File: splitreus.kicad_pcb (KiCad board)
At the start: 2 copper layers, 134.3 x 107.2 mm, 97 parts, among them J1 TRRS, J2 battery, SW0 SW_PUSH, SW1 SW_PUSH, SW10 SW_PUSH, SW11 SW_PUSH, SW12 SW_PUSH, SW13 SW_PUSH, SW14 SW_PUSH, SW15 SW_PUSH, SW16 SW_PUSH, SW17 SW_PUSH, SW18 SW_PUSH, SW19 SW_PUSH, SW2 SW_PUSH, SW20 SW_PUSH, SW21 SW_PUSH, SW22 SW_PUSH, SW23 SW_PUSH, SW24 SW_PUSH, SW25 SW_PUSH, SW26 SW_PUSH, SW27 SW_PUSH, SW28 SW_PUSH, SW29 SW_PUSH, SW3 SW_PUSH, SW30 SW_PUSH, SW4 SW_PUSH, SW5 SW_PUSH, SW6 SW_PUSH, SW7 SW_PUSH, SW8 SW_PUSH, SW9 SW_PUSH, U1 ProMicro

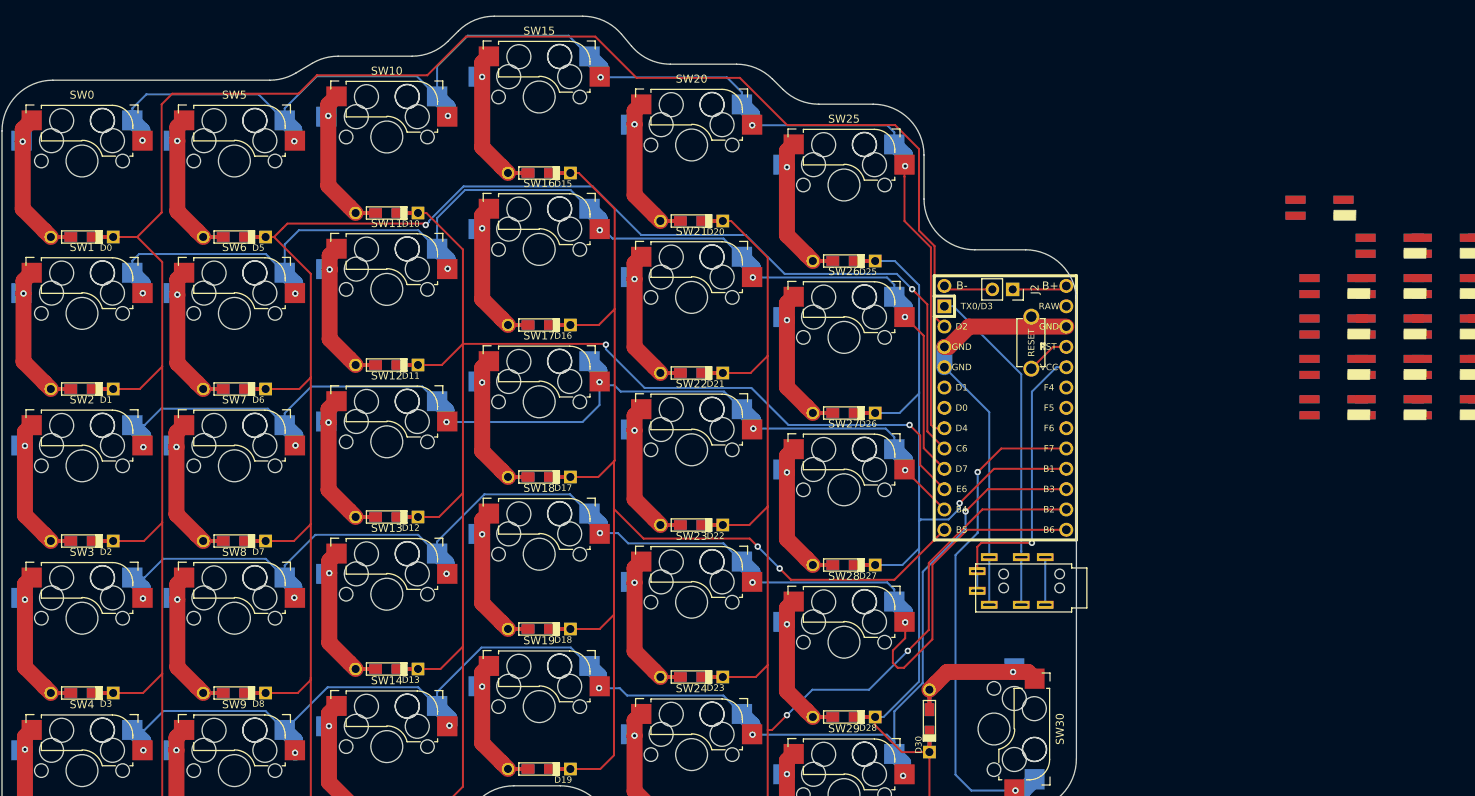
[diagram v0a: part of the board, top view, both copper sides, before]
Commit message: leds and placements
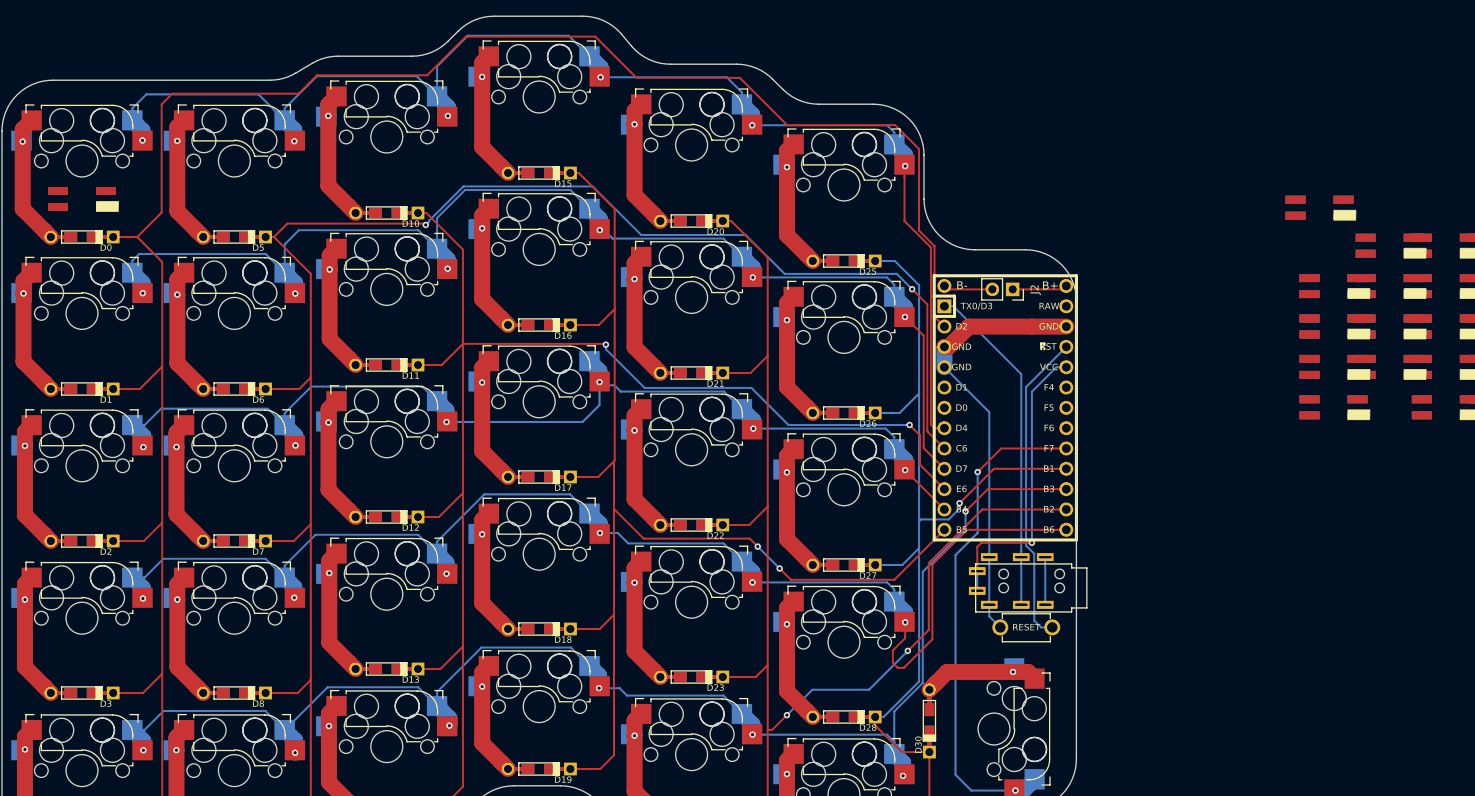
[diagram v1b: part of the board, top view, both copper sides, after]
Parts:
- moved D90 165.5 mm to (0.00, 4.75)
- moved RST1 35.6 mm to (118.0, 58.3), turned to 180 degrees
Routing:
- net RST: track 5.70 -> 39.5 mm
- net GND: track 52.1 -> 54.3 mm

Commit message: leds
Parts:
- moved D94 176.0 mm to (0.00, 81.0)
- moved D99 173.4 mm to (19.1, 81.0)
- moved D92 166.6 mm to (0.00, 42.9)
- moved D93 161.8 mm to (0.00, 61.9)
- moved D91 156.7 mm to (0.00, 23.8)
- moved D98 153.9 mm to (19.1, 42.9)
- moved D95 151.5 mm to (19.1, 4.75)
- moved D97 146.1 mm to (19.1, 42.9)
- moved D96 137.4 mm to (19.1, 23.8)
- moved D912 133.8 mm to (38.1, 39.9)
- moved D910 121.8 mm to (38.1, 1.75)
- moved D916 117.5 mm to (38.1, 20.8)
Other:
- outline, holes or cut-outs redrawn

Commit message: holes and leds
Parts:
- added U1: HOLE, MountingHole:MountingHole_2.2mm_M2_DIN965_Pad, F.Cu at (28.6, 27.1)
- added U2: HOLE, MountingHole:MountingHole_2.2mm_M2_DIN965_Pad, F.Cu at (28.6, 65.2)
- added U3: HOLE, MountingHole:MountingHole_2.2mm_M2_DIN965_Pad, F.Cu at (85.7, 29.1)
- added U4: HOLE, MountingHole:MountingHole_2.2mm_M2_DIN965_Pad, F.Cu at (85.7, 67.2)
- moved D914 161.2 mm to (38.1, 78.0)
- moved D919 148.2 mm to (57.1, 73.0)
- moved D913 146.0 mm to (38.1, 58.9)
- moved D924 140.2 mm to (76.2, 79.0)
- moved D918 133.0 mm to (57.1, 53.9)
- moved D911 125.5 mm to (38.1, 20.8)
- moved D923 123.5 mm to (76.2, 59.9)
- moved D917 121.2 mm to (57.1, 34.9)
- moved D915 117.0 mm to (57.1, -3.25)
- moved D928 114.5 mm to (95.2, 64.9)
- moved D922 110.2 mm to (76.2, 40.9)
- moved D929 103.9 mm to (95.2, 84.0)
- moved D921 101.4 mm to (76.2, 21.8)
- moved D927 99.5 mm to (95.2, 45.9)
- moved D920 98.4 mm to (76.2, 2.75)
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- renumbered U1 to U0
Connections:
- D930 pad 3: Net-(D925-Pad1) -> Net-(D930-Pad3)
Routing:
- net COL4: track 155.1 -> 158.8 mm
- net COL2: track 172.3 -> 175.8 mm
- net COL1: track 210.4 -> 207.8 mm
- net ROW5: track 62.6 -> 64.3 mm
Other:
- outline, holes or cut-outs redrawn

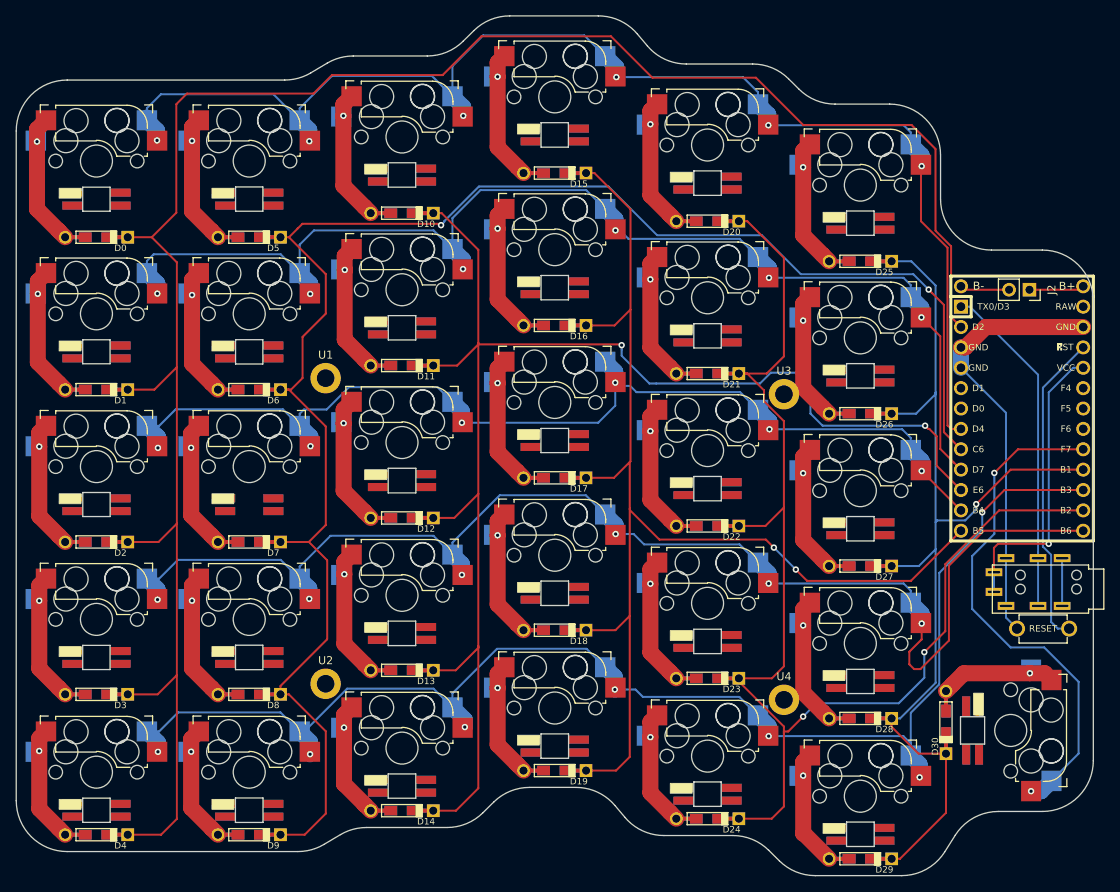
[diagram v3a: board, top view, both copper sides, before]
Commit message: auto route leds
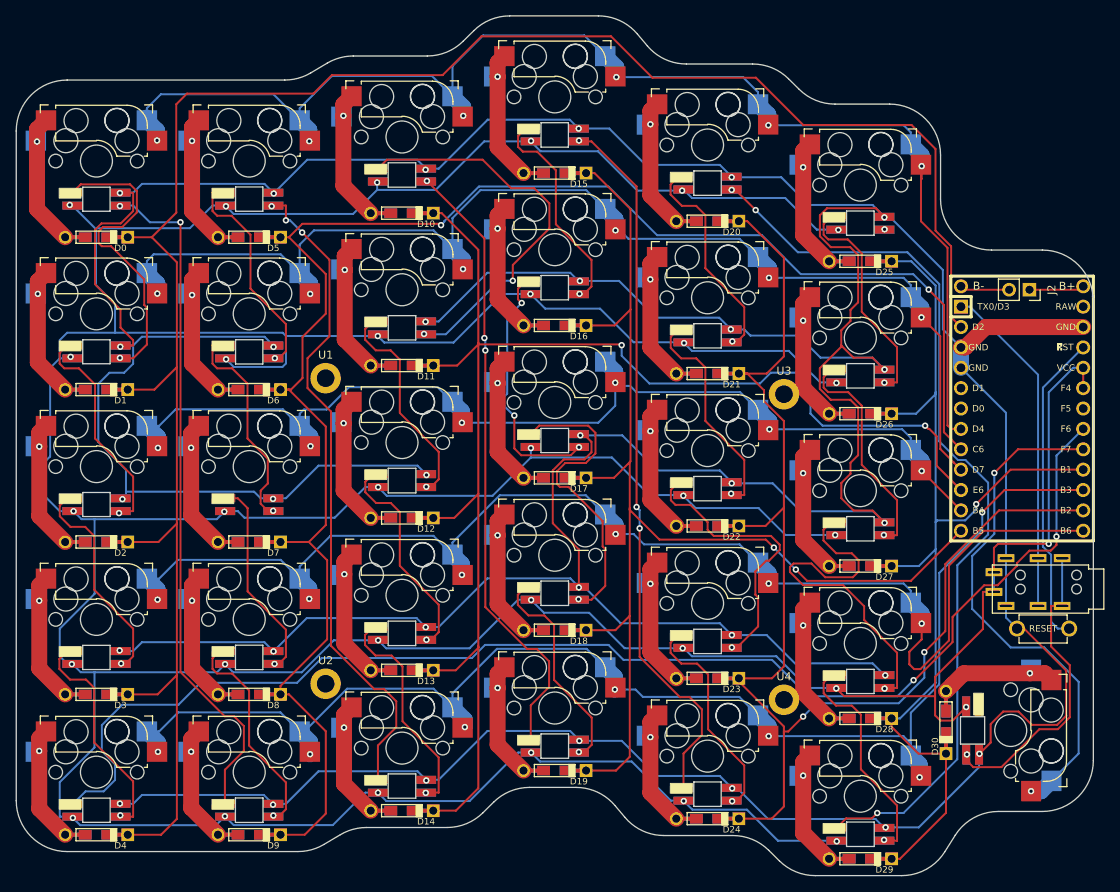
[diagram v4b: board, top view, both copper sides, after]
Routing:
- net GND: track 54.3 -> 754.3 mm, vias 0 -> 31
- net VCC: track 37.0 -> 705.4 mm, vias 1 -> 32
- net LED: track 0.00 -> 165.9 mm, vias 0 -> 3
- net Net-(D920-Pad1): track 0.00 -> 113.5 mm, vias 0 -> 4
- net Net-(D915-Pad1): track 0.00 -> 89.9 mm, vias 0 -> 4
- net Net-(D90-Pad1): track 0.00 -> 86.3 mm, vias 0 -> 3
- net Net-(D914-Pad3): track 0.00 -> 83.7 mm, vias 0 -> 4
- net Net-(D910-Pad1): track 0.00 -> 78.2 mm, vias 0 -> 4
- net Net-(D910-Pad3): track 0.00 -> 49.9 mm, vias 0 -> 3
- net Net-(D927-Pad3): track 0.00 -> 45.4 mm, vias 0 -> 2
- net Net-(D917-Pad3): track 0.00 -> 38.9 mm, vias 0 -> 2
- net Net-(D90-Pad3): track 0.00 -> 38.8 mm, vias 0 -> 2
- net Net-(D922-Pad3): track 0.00 -> 36.1 mm, vias 0 -> 2
- net to_right: track 5.95 -> 38.9 mm, vias 0 -> 1
- net Net-(D916-Pad3): track 0.00 -> 32.6 mm, vias 0 -> 4
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
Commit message: changes
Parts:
- added SW1: SW_SPDT, nrfmicro:switch_MSK-12C02_smd, B.Cu at (113.5, 11.4)
- moved J2 2.10 mm to (116.3, 18.1)
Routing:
- net B+: track 6.88 -> 0.61 mm
- net B-: track 6.18 -> 7.66 mm
- net ROW3: track 166.3 -> 165.6 mm
- net Net-(D24-Pad1): track 20.1 -> 20.7 mm
- net Net-(D4-Pad1): track 20.0 -> 20.7 mm
- net Net-(D19-Pad1): track 20.0 -> 20.7 mm
- net Net-(D9-Pad1): track 20.0 -> 20.6 mm
- net Net-(D14-Pad1): track 20.0 -> 20.7 mm
- net Net-(D29-Pad1): track 20.1 -> 20.7 mm

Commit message: update
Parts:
- SW1: footprint nrfmicro:switch_MSK-12C02_smd -> Custom Footies:reversible_power; moved to F.Cu
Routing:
- net (no net): vias 0 -> 3
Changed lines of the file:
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@@
     (thickness 1.6)
     (drawings 580)
-    (tracks 2370)
+    (tracks 2373)
     (zones 0)
     (modules 102)
@@
     (40 Dwgs.User user)
     (41 Cmts.User user hide)
-    (42 Eco1.User user)
+    (42 Eco1.User user hide)
     (43 Eco2.User user)
     (44 Edge.Cuts user)
@@
   )
   (setup
-    (last_trace_width 2)
+    (last_trace_width 0.25)
     (user_trace_width 2)
     (trace_clearance 0.2)
@@
     (add_net to_right)
   )
-  (module nrfmicro:switch_MSK-12C02_smd (layer B.Cu)
+  (module "Custom Footies:reversible_power" (layer F.Cu)
     (at 113.548 11.428 270)
     (attr smd)
-    (fp_text reference SW1 (at 1.35 0) (layer B.Fab)
-      (effects (font (size 1 1) (thickness 0.15)) (justify mirror))
+    (fp_text reference SW1 (at 1.35 0) (layer F.Fab)
+      (effects (font (size 1 1) (thickness 0.15)))
     )
-    (fp_text value SW_SPDT (at 5.35 0) (layer B.Fab)
-      (effects (font (size 1 1) (thickness 0.15)) (justify mirror))
+    (fp_text value SW_SPDT (at 5.35 0) (layer F.Fab)
+      (effects (font (size 1 1) (thickness 0.15)))
     )
-    (fp_line (start 0.3 1.5) (end 0 1.5) (layer Dwgs.User) (width 0.15))
     (fp_line (start 0.3 -1.5) (end 0 -1.5) (layer Dwgs.User) (width 0.15))
-    (fp_line (start 0.3 -1.5) (end 0.3 1.5) (layer Dwgs.User) (width 0.15))
-    (fp_line (start -1.5 0.2) (end -1.5 1.5) (layer Dwgs.User) (width 0.15))
-    (fp_line (start 0 0.2) (end -1.5 0.2) (layer Dwgs.User) (width 0.15))
-    (fp_line (start -1.5 1.5) (end 0 1.5) (layer Dwgs.User) (width 0.15))
-    (fp_line (start 0 -3.3) (end 2.7 -3.3) (layer Dwgs.User) (width 0.15))
-    (fp_line (start 0 3.3) (end 0 -3.3) (layer Dwgs.User) (width 0.15))
-    (fp_line (start 2.7 3.3) (end 2.7 -3.3) (layer Dwgs.User) (width 0.15))
+    (fp_line (start 0.3 1.5) (end 0 1.5) (layer Dwgs.User) (width 0.15))
+    (fp_line (start 0.3 1.5) (end 0.3 -1.5) (layer Dwgs.User) (width 0.15))
+    (fp_line (start -1.5 -0.2) (end -1.5 -1.5) (layer Dwgs.User) (width 0.15))
+    (fp_line (start 0 -0.2) (end -1.5 -0.2) (layer Dwgs.User) (width 0.15))
+    (fp_line (start -1.5 -1.5) (end 0 -1.5) (layer Dwgs.User) (width 0.15))
     (fp_line (start 0 3.3) (end 2.7 3.3) (layer Dwgs.User) (width 0.15))
-    (pad "" smd rect (at 2.493 -3.6 180) (size 1 0.6) (layers B.Cu B.Paste B.Mask))
-    (pad "" smd rect (at 0.207 -3.6 180) (size 1.1 0.6) (layers B.Cu B.Paste B.Mask))
-    (pad "" smd rect (at 2.493 3.6 180) (size 1.1 0.6) (layers B.Cu B.Paste B.Mask))
-    (pad "" np_thru_hole circle (at 1.35 1.45 90) (size 0.7 0.7) (drill 0.7) (layers *.Cu *.Mask))
+    (fp_line (start 0 -3.3) (end 0 3.3) (layer Dwgs.User) (width 0.15))
+    (fp_line (start 2.7 -3.3) (end 2.7 3.3) (layer Dwgs.User) (width 0.15))
+    (fp_line (start 0 -3.3) (end 2.7 -3.3) (layer Dwgs.User) (width 0.15))
+    (pad "" smd rect (at 2.483 -3.6) (size 1.1 0.6) (layers B.Cu B.Paste B.Mask))
+    (pad "" smd rect (at 0.207 -3.6) (size 1 0.6) (layers B.Cu B.Paste B.Mask))
+    (pad "" smd rect (at 0.207 3.6) (size 1.1 0.6) (layers B.Cu B.Paste B.Mask))
+    (pad "" smd rect (at 2.493 3.6) (size 1 0.6) (layers B.Cu B.Paste B.Mask))
+    (pad 3 smd rect (at 3.2 2.2 90) (size 1 0.6) (layers B.Cu B.Paste B.Mask))
+    (pad 2 smd rect (at 3.2 0.7 90) (size 1 0.6) (layers B.Cu B.Paste B.Mask))
+    (pad 1 smd rect (at 3.2 -2.2 90) (size 1 0.6) (layers F.Cu F.Paste F.Mask))
+    (pad "" smd rect (at 2.493 3.6) (size 1 0.6) (layers F.Cu F.Paste F.Mask))
+    (pad "" smd rect (at 0.207 3.6) (size 1.1 0.6) (layers F.Cu F.Paste F.Mask))
+    (pad "" smd rect (at 2.493 -3.6) (size 1.1 0.6) (layers F.Cu F.Paste F.Mask))
     (pad "" np_thru_hole circle (at 1.35 -1.45 90) (size 0.7 0.7) (drill 0.7) (layers *.Cu *.Mask))
-    (pad 2 smd rect (at 3.2 -0.7 90) (size 1 0.6) (layers B.Cu B.Paste B.Mask))
-    (pad 3 smd rect (at 3.2 -2.2 90) (size 1 0.6) (layers B.Cu B.Paste B.Mask))
-    (pad 1 smd rect (at 3.2 2.2 90) (size 1 0.6) (layers B.Cu B.Paste B.Mask))
-    (pad "" smd rect (at 0.207 3.6 180) (size 1 0.6) (layers B.Cu B.Paste B.Mask))
+    (pad "" np_thru_hole circle (at 1.35 1.45 90) (size 0.7 0.7) (drill 0.7) (layers *.Cu *.Mask))
+    (pad 2 smd rect (at 3.2 0.7 90) (size 1 0.6) (layers F.Cu F.Paste F.Mask))
+    (pad 3 smd rect (at 3.2 2.2 90) (size 1 0.6) (layers F.Cu F.Paste F.Mask))
+    (pad 1 smd rect (at 3.2 -2.2 90) (size 1 0.6) (layers B.Cu B.Adhes B.Mask))
+    (pad "" smd rect (at 0.207 -3.6) (size 1 0.6) (layers F.Cu F.Paste F.Mask))
     (model ${KISYS3DMOD}/Button_Switch_SMD.3dshapes/SW_SPDT_PCM12.wrl
       (offset (xyz 1.7 0 0))
@@
   (gr_line (start -7.75 82.4) (end -7.75 69.6) (layer Cmts.User) (width 0.1))
   (gr_line (start 7.75 82.4) (end -7.75 82.4) (layer Cmts.User) (width 0.1))
+  (via (at 115.738 14.578) (size 0.8) (drill 0.4) (layers F.Cu B.Cu) (net 0))
+  (via (at 112.818 14.598) (size 0.8) (drill 0.4) (layers F.Cu B.Cu) (net 0))
+  (via (at 111.348 14.628) (size 0.8) (drill 0.4) (layers F.Cu B.Cu) (net 0))
   (segment (start -2.45 9.5) (end -3.9 9.5) (width 0.25) (layer B.Cu) (net 1))
   (segment (start -1.4 9.5) (end -2.45 9.5) (width 0.25) (layer B.Cu) (net 1))

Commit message: fin?
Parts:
- removed the SW1 at (113.5, 11.4)
- added G***: LOGO, Custom Footies:sp62, F.Cu at (52.5, 25.2)
- added SW91: SW_SPDT, Custom Footies:reversible_power, F.Cu at (114.4, 11.4)
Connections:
- U0 pad B+: B+ -> V+
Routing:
- net V+: track 0.00 -> 7.86 mm, vias 0 -> 1
- net B+: track 0.61 -> 4.71 mm, vias 0 -> 1
- net Net-(SW91-Pad3): vias 0 -> 1
- net (no net): vias 3 -> 0
- added copper zone on B.Cu, net (none)
- added copper zone on F.Cu, net (none)
